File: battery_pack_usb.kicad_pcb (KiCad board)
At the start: 2 copper layers, 30.4 x 15 mm, 25 parts, among them J1 Conn_01x02_Male, J2 USB_C_Receptacle_USB2.0, SW1 SW_SPST, U1 BQ25886

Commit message: Update to KiCad 5.1.7
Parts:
- C1: value 1u -> 1u 5V
- C2, C3: value 10u -> 10u 5V
- C6: value 10u -> 10u 9V
- C7, C8: value 22u -> 22u 9V
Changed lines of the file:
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@@
-(kicad_pcb (version 20171130) (host pcbnew 5.1.6-c6e7f7d~87~ubuntu18.04.1)
+(kicad_pcb (version 20171130) (host pcbnew 5.1.7-a382d34a8~87~ubuntu20.04.1)
   (general
     (thickness 1.6)
@@
   )
   (setup
-    (last_trace_width 0.15)
+    (last_trace_width 0.25)
     (user_trace_width 0.15)
     (user_trace_width 0.5)
@@
       (effects (font (size 0.8 0.8) (thickness 0.1)))
     )
-    (fp_text value 22u (at 0 1.65 90) (layer F.Fab)
+    (fp_text value "22u 9V" (at 0 1.65 90) (layer F.Fab)
       (effects (font (size 1 1) (thickness 0.15)))
     )
@@
     )
     (fp_text value Battery (at 0 4.87) (layer F.Fab)
-      (effects (font (size 1 1) (thickness 0.15)))
-    )
-    (fp_text user %R (at 0 1.27 90) (layer F.Fab)
       (effects (font (size 1 1) (thickness 0.15)))
     )
@@
     (fp_line (start 1.8 4.35) (end 1.8 -1.8) (layer F.CrtYd) (width 0.05))
     (fp_line (start 1.8 -1.8) (end -1.8 -1.8) (layer F.CrtYd) (width 0.05))
+    (fp_text user %R (at 0 1.27 90) (layer F.Fab)
+      (effects (font (size 1 1) (thickness 0.15)))
+    )
     (fp_text user BAT (at 0 -2.286 180) (layer F.SilkS)
       (effects (font (size 0.8 0.8) (thickness 0.1)))
@@
       (effects (font (size 0.8 0.8) (thickness 0.1)))
     )
-    (fp_text value 22u (at 0 1.65 90) (layer F.Fab)
+    (fp_text value "22u 9V" (at 0 1.65 90) (layer F.Fab)
       (effects (font (size 1 1) (thickness 0.15)))
     )
@@
       (effects (font (size 0.8 0.8) (thickness 0.1)))
     )
-    (fp_text value 10u (at 0 1.65) (layer F.Fab)
+    (fp_text value "10u 9V" (at 0 1.65) (layer F.Fab)
       (effects (font (size 1 1) (thickness 0.15)))
     )
@@
       (effects (font (size 0.8 0.8) (thickness 0.1)))
     )
-    (fp_text value 10u (at 0 1.65 90) (layer F.Fab)
+    (fp_text value "10u 5V" (at 0 1.65 90) (layer F.Fab)
       (effects (font (size 1 1) (thickness 0.15)))
     )
@@
       (effects (font (size 0.8 0.8) (thickness 0.1)))
     )
-    (fp_text value 10u (at 0 1.65 90) (layer F.Fab)
+    (fp_text value "10u 5V" (at 0 1.65 90) (layer F.Fab)
       (effects (font (size 1 1) (thickness 0.15)))
     )
@@
       (effects (font (size 0.8 0.8) (thickness 0.1)))
     )
-    (fp_text value 1u (at 0 1.43 90) (layer F.Fab)
+    (fp_text value "1u 5V" (at 0 1.43 90) (layer F.Fab)
       (effects (font (size 1 1) (thickness 0.15)))
     )
@@
   (gr_line (start 133.985 109.982) (end 133.985 121.412) (layer Edge.Cuts) (width 0.05))
   (gr_line (start 105.41 108.204) (end 132.207 108.204) (layer Edge.Cuts) (width 0.05))
-  (via (at 120.65 120.396) (size 0.8) (drill 0.4) (layers F.Cu B.Cu) (net 2))
-  (via (at 122.682 120.396) (size 0.8) (drill 0.4) (layers F.Cu B.Cu) (net 2))
-  (via (at 117.602 120.65) (size 0.8) (drill 0.4) (layers F.Cu B.Cu) (net 2))
-  (via (at 127.762 118.618) (size 0.8) (drill 0.4) (layers F.Cu B.Cu) (net 2))
-  (via (at 128.778 116.84) (size 0.8) (drill 0.4) (layers F.Cu B.Cu) (net 2))
-  (via (at 124.206 121.92) (size 0.8) (drill 0.4) (layers F.Cu B.Cu) (net 2))
   (segment (start 125.8085 118.045) (end 124.8575 117.094) (width 0.5) (layer F.Cu) (net 1))
   (segment (start 125.8085 118.745) (end 125.8085 118.045) (width 0.5) (layer F.Cu) (net 1))
@@
   (segment (start 127.2055 120.142) (end 131.699 120.142) (width 0.5) (layer F.Cu) (net 1))
   (segment (start 125.8085 118.745) (end 127.2055 120.142) (width 0.5) (layer F.Cu) (net 1))
+  (via (at 120.65 120.396) (size 0.8) (drill 0.4) (layers F.Cu B.Cu) (net 2))
+  (via (at 122.682 120.396) (size 0.8) (drill 0.4) (layers F.Cu B.Cu) (net 2))
+  (via (at 117.602 120.65) (size 0.8) (drill 0.4) (layers F.Cu B.Cu) (net 2))
+  (via (at 127.762 118.618) (size 0.8) (drill 0.4) (layers F.Cu B.Cu) (net 2))
+  (via (at 128.778 116.84) (size 0.8) (drill 0.4) (layers F.Cu B.Cu) (net 2))
+  (via (at 124.206 121.92) (size 0.8) (drill 0.4) (layers F.Cu B.Cu) (net 2))
   (segment (start 121.203 114.5135) (end 121.453 114.7635) (width 0.25) (layer F.Cu) (net 2))
   (segment (start 120.4405 114.5135) (end 121.203 114.5135) (width 0.25) (layer F.Cu) (net 2))

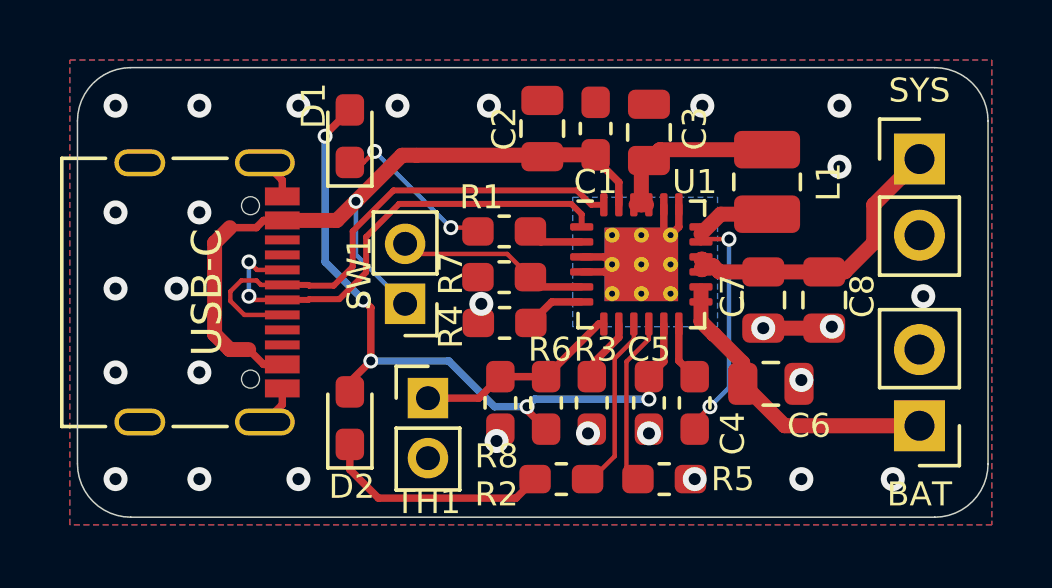
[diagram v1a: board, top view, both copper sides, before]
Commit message: Convert to KiCad 7.0.8
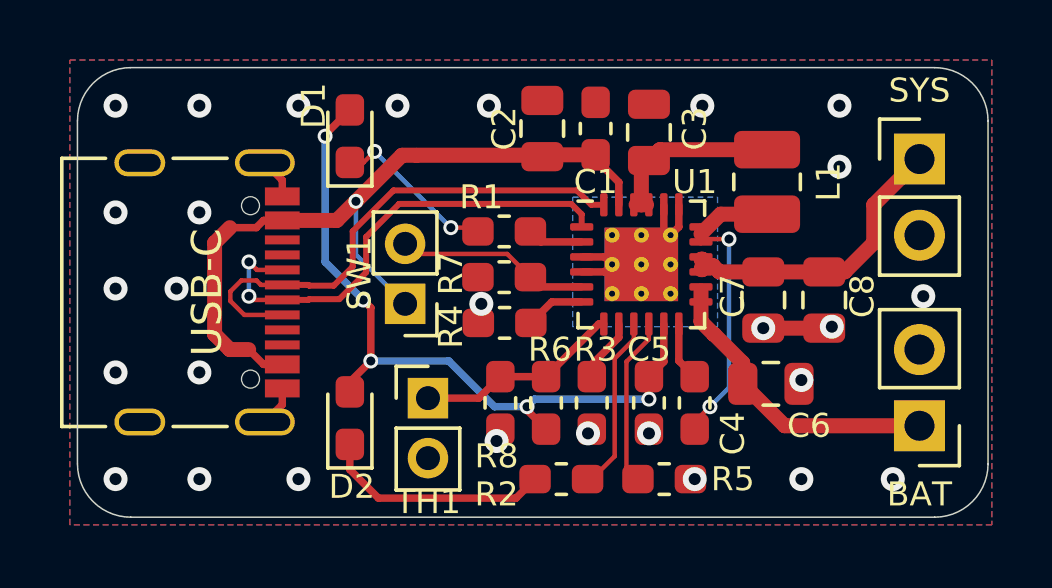
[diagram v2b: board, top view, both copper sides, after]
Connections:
- J2 pad A5: (no net) -> unconnected-(J2-CC1-PadA5)
- J2 pad A8: (no net) -> unconnected-(J2-SBU1-PadA8)
- J2 pad B5: (no net) -> unconnected-(J2-CC2-PadB5)
- J2 pad B8: (no net) -> unconnected-(J2-SBU2-PadB8)
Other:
- net class Default removed

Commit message: Improve circuit and PCB
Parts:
- removed SW1: SW_SPST, Connector_PinHeader_2.00mm:PinHeader_1x02_P2.00mm_Vertical
- added D3: Green, Connector_Molex:Molex_PicoBlade_53047-0210_1x02_P1.25mm_Vertical, F.Cu at (109.6, 94.0)
- added D4: ESD5Zxx, Diode_SMD:D_SOD-523, F.Cu at (103.2, 93.8)
- added D5: ESD5Zxx, Diode_SMD:D_SOD-523, F.Cu at (106.8, 98.2)
- added D6: ESD5Zxx, Diode_SMD:D_SOD-523, F.Cu at (106.8, 102.0)
- added H1: MountingHole, MountingHole:MountingHole_3.2mm_M3_ISO14580, F.Cu at (111.0, 100.0)
- added H2: MountingHole, MountingHole:MountingHole_3.2mm_M3_ISO14580, F.Cu at (137.0, 100.0)
- added R10: 5k1, Resistor_SMD:R_0603_1608Metric_Pad0.98x0.95mm_HandSolder, F.Cu at (105.0, 97.8)
- added R9: 5k1, Resistor_SMD:R_0603_1608Metric_Pad0.98x0.95mm_HandSolder, F.Cu at (105.0, 102.8)
- BT1: footprint Connector_PinHeader_2.54mm:PinHeader_1x02_P2.54mm_Vertical -> Connector_Molex:Molex_PicoBlade_53047-0210_1x02_P1.25mm_Vertical
- C1: value 1u 5V -> 1u; footprint Capacitor_SMD:C_0603_1608Metric_Pad1.05x0.95mm_HandSolder -> Capacitor_SMD:C_0603_1608Metric_Pad1.08x0.95mm_HandSolder
- C2, C3: value 10u 5V -> 10u; footprint Capacitor_SMD:C_0805_2012Metric -> Capacitor_SMD:C_0805_2012Metric_Pad1.18x1.45mm_HandSolder
- C4, C5: footprint Capacitor_SMD:C_0603_1608Metric_Pad1.05x0.95mm_HandSolder -> Capacitor_SMD:C_0603_1608Metric_Pad1.08x0.95mm_HandSolder
- C6: value 10u 9V -> 10u 10V; footprint Capacitor_SMD:C_0805_2012Metric -> Capacitor_SMD:C_0805_2012Metric_Pad1.18x1.45mm_HandSolder
- C7, C8: value 22u 9V -> 22u 10V; footprint Capacitor_SMD:C_0805_2012Metric -> Capacitor_SMD:C_0805_2012Metric_Pad1.18x1.45mm_HandSolder
- D1: value LED -> Red; footprint LED_SMD:LED_0603_1608Metric_Pad1.05x0.95mm_HandSolder -> Connector_Molex:Molex_PicoBlade_53047-0210_1x02_P1.25mm_Vertical
- D2: value LED -> Blue
- J1: value Conn_01x02_Male -> Output; footprint Connector_PinHeader_2.54mm:PinHeader_1x02_P2.54mm_Vertical -> Connector_Molex:Molex_PicoBlade_53047-0210_1x02_P1.25mm_Vertical
- J2: value USB_C_Receptacle_USB2.0 -> USB_C_Receptacle_USB2.0_16P
- L1: value 1u -> 1u (XGL3515-102); footprint Inductor_SMD:L_1008_2520Metric -> extraFootprints:XxL3515
- R1, R2, R3, R4, R6, R8: footprint Resistor_SMD:R_0603_1608Metric_Pad1.05x0.95mm_HandSolder -> Resistor_SMD:R_0603_1608Metric_Pad0.98x0.95mm_HandSolder
- R5: value 7k5 -> 4k7; footprint Resistor_SMD:R_0603_1608Metric_Pad1.05x0.95mm_HandSolder -> Resistor_SMD:R_0603_1608Metric_Pad0.98x0.95mm_HandSolder
- R7: value 10k -> R; footprint Resistor_SMD:R_0603_1608Metric_Pad1.05x0.95mm_HandSolder -> Resistor_SMD:R_0603_1608Metric_Pad0.98x0.95mm_HandSolder
- TH1: footprint Connector_PinHeader_2.00mm:PinHeader_1x02_P2.00mm_Vertical -> Connector_Molex:Molex_PicoBlade_53047-0210_1x02_P1.25mm_Vertical
- moved C4 23.6 mm to (128.5, 96.2), turned to 90 degrees
- moved D2 19.4 mm to (127.1, 106.8), turned to 180 degrees
- moved L1 18.7 mm to (123.9, 93.5), turned to 0 degrees
- moved J2 17.6 mm to (100.0, 100.0)
- moved J1 17.1 mm to (133.2, 94.2), turned to 180 degrees
- moved D1 16.6 mm to (115.1, 94.0), turned to 180 degrees
- moved R1 16.4 mm to (115.7, 97.4), turned to 180 degrees
- moved R7 16.4 mm to (116.0, 98.9)
- moved C8 16.1 mm to (130.9, 100.0), turned to 90 degrees
- moved C7 16.1 mm to (128.7, 100.0), turned to 90 degrees
- moved R5 15.9 mm to (122.9, 106.0), turned to 90 degrees
- moved R2 15.3 mm to (127.1, 108.5), turned to 180 degrees
- moved C6 15.0 mm to (126.4, 103.8), turned to -90 degrees
- moved C2 14.5 mm to (119.2, 95.8), turned to 180 degrees
- moved BT1 14.2 mm to (133.8, 106.0)
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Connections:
- net /SYS renamed Net-(J1-Pin_1)
- C1 pad 1: GND -> /V_{Bus}
- C1 pad 2: Net-(SW1-A) -> GND
- C2 pad 1: GND -> /V_{Bus}
- C2 pad 2: Net-(SW1-A) -> GND
- D1 pad 2: /REGN -> /V_{Bus}
- J2 pad A4: Net-(SW1-A) -> /V_{Bus}
- J2 pad A5: unconnected-(J2-CC1-PadA5) -> Net-(J2-CC1)
- J2 pad A9: Net-(SW1-A) -> /V_{Bus}
- J2 pad B4: Net-(SW1-A) -> /V_{Bus}
- J2 pad B5: unconnected-(J2-CC2-PadB5) -> Net-(J2-CC2)
- J2 pad B9: Net-(SW1-A) -> /V_{Bus}
- R1 pad 1: Net-(D1-K) -> Net-(U1-STAT)
- R1 pad 2: Net-(U1-STAT) -> Net-(D1-K)
- R7 pad 1: Net-(SW1-B) -> Net-(U1-STAT)
- R7 pad 2: GND -> Net-(D3-A)
- U1 pad 23: Net-(SW1-A) -> /V_{Bus}
- U1 pad 5: Net-(SW1-B) -> GND
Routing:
- net /V_{Bus}: track 0.00 -> 37.9 mm
- net Net-(SW1-A): track 25.8 -> 0.00 mm, vias 1 -> 0
- net GND: track 12.0 -> 29.7 mm, vias 28 -> 65
- net /REGN: track 24.4 -> 10.8 mm, vias 5 -> 2
- net /D-: track 16.1 -> 27.2 mm
- net Net-(U1-BTST): track 1.97 -> 11.9 mm, vias 0 -> 2
- net /D+: track 17.1 -> 26.8 mm
- net Net-(J1-Pin_1): track 10.1 -> 18.8 mm
- net Net-(D3-A): track 0.00 -> 8.17 mm
- net Net-(SW1-B): track 6.48 -> 0.00 mm
- net Net-(D2-K): track 7.67 -> 1.66 mm
- net Net-(U1-TS): track 6.89 -> 12.3 mm
- net Net-(U1-ICHGSET): track 5.64 -> 1.69 mm
- net Net-(U1-STAT): track 1.85 -> 5.42 mm, vias 0 -> 2
- net BAT: track 10.2 -> 13.4 mm
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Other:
- board size 30.4 x 15 mm -> 44 x 19 mm
- rule pad_to_mask_clearance: 0.05 -> 0
- board text added: "2S USB-C Li-Ion charger v1.1 2024-06 by MG-5"
- board text added: "JLCJLCJLCJLC"
- board text removed: "2S-USB-Charger V1.0 by MG 2020-08"
